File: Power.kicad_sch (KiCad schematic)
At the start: 2 parts, among them U1 LM5155DSSR, U2 LM5155DSSR

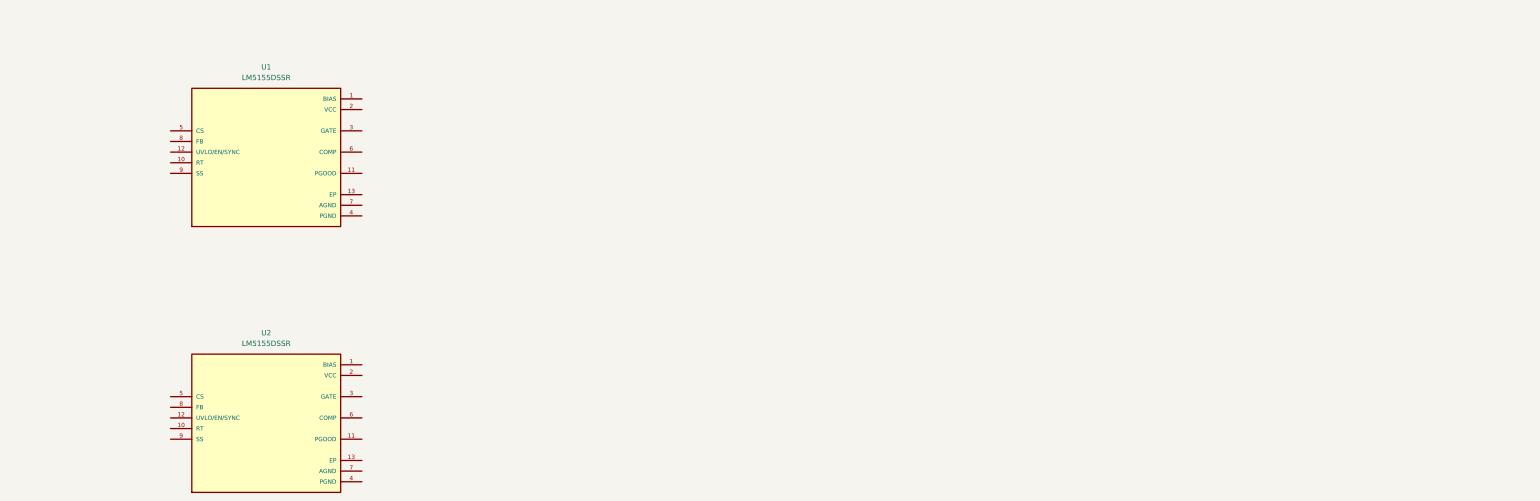
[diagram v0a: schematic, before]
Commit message: finished SOM 5V power, migrated altium stuff, finished pin study, added USB PHY (revise HS capability)
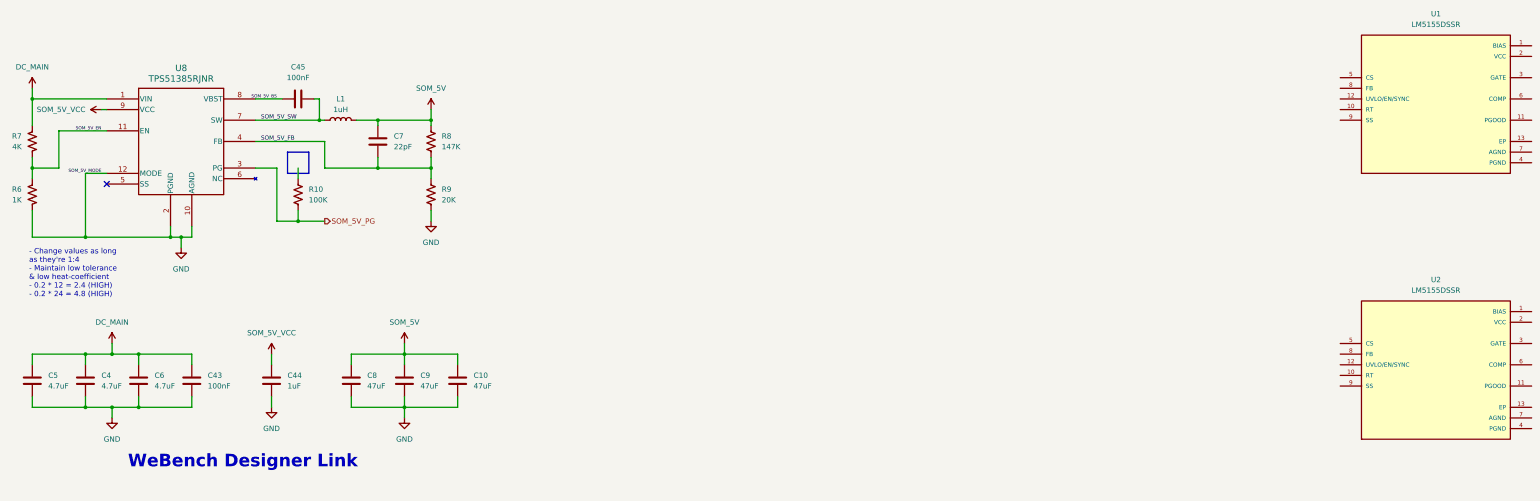
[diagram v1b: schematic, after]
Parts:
- added C10, C8, C9: 47uF, symbol Device:C
- added C4, C5, C6: 4.7uF, symbol Device:C
- added C43, C45: 100nF, symbol Device:C
- added C44: 1uF, symbol Device:C
- added C7: 22pF, symbol Device:C
- added L1: 1uH, symbol Device:L
- added R10: 100K, symbol Device:R_US
- added R6: 1K, symbol Device:R_US
- added R7: 4K, symbol Device:R_US
- added R8: 147K, symbol Device:R_US
- added R9: 20K, symbol Device:R_US
- added U8: TPS51385RJNR, VQFN-HR12_RJN_TEX, symbol TPS51385RJNR:TPS51385RJNR
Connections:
- new net DC_MAIN: C4.1, C43.1, C5.1, C6.1, R7.1, U8.1 (VIN)
- new net GND: C10.2, C4.2, C43.2, C44.2, C5.2, C6.2, C8.2, C9.2, R6.2, R9.2, U8.10 (AGND), U8.12 (MODE), U8.2 (PGND)
- new net SOM_5V: C10.1, C7.1, C8.1, C9.1, L1.2, R8.1
- new net SOM_5V_BS: C45.1, U8.8 (VBST)
- new net SOM_5V_EN: R6.1, R7.2, U8.11 (EN)
- new net SOM_5V_FB: C7.2, R8.2, R9.1, U8.4 (FB)
- new net SOM_5V_PG: R10.2, U8.3 (PG)
- new net SOM_5V_SW: C45.2, L1.1, U8.7 (SW)
- new net SOM_5V_VCC: C44.1, U8.9 (VCC)
- no-connect marks 0 -> 1
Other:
- note added: "- Change values as long as they're 1:4 - Maintain low tolerance & low heat-coefficient - 0.2 * 12 = 2.4 (HIGH) - 0.2 * 24 = 4.8 (HIGH)"
- note added: "WeBench Designer Link"
- moved on the sheet: U1, U2

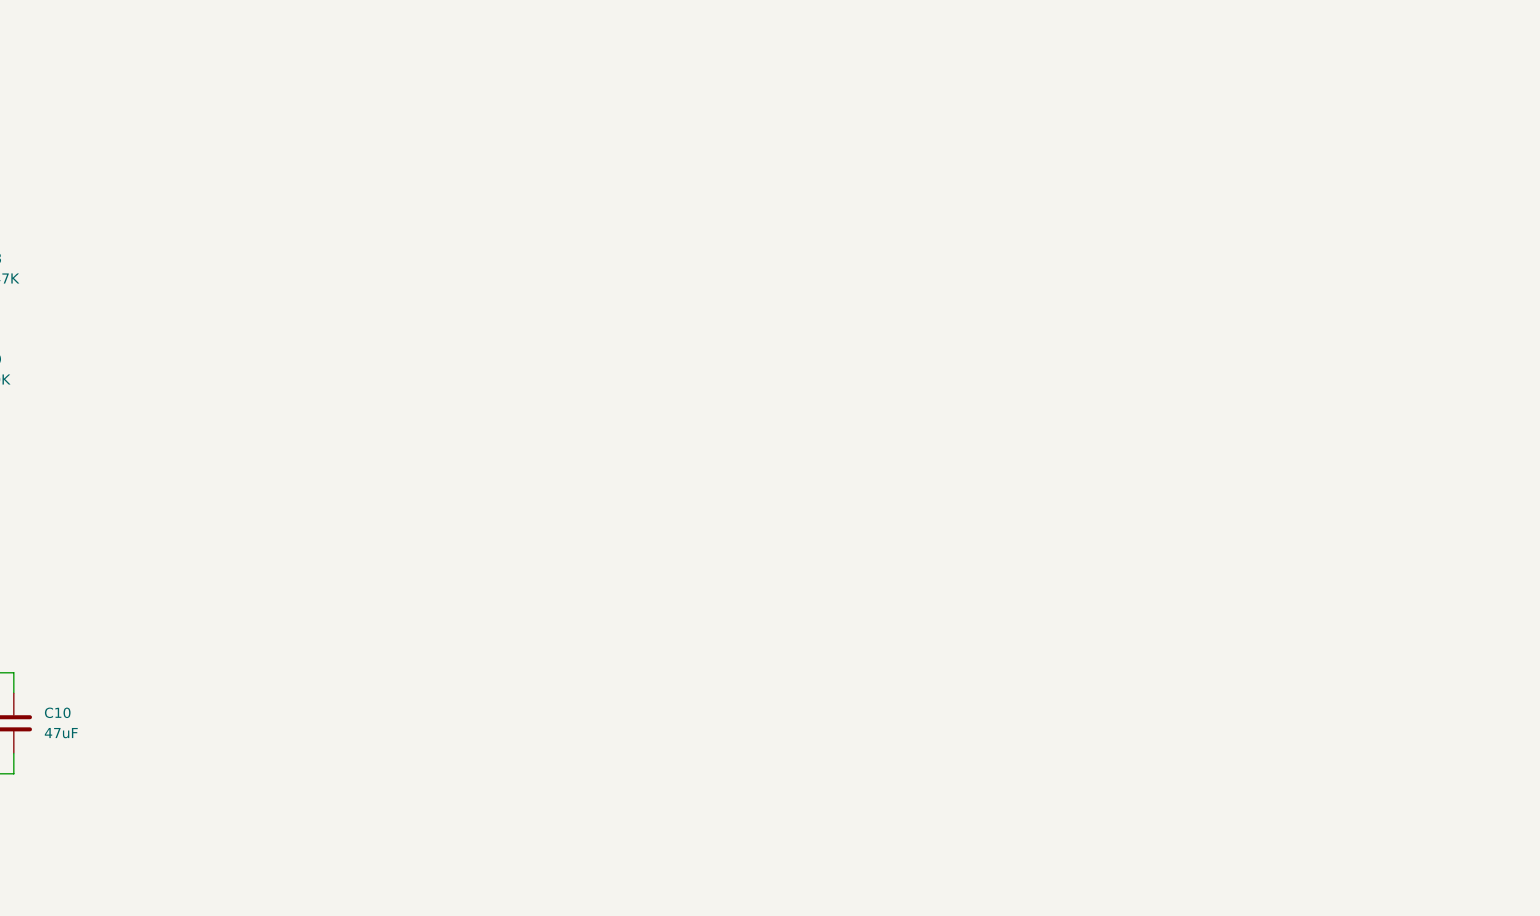
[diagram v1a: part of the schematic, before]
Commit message: added ADC clock fanout, added 3A buck
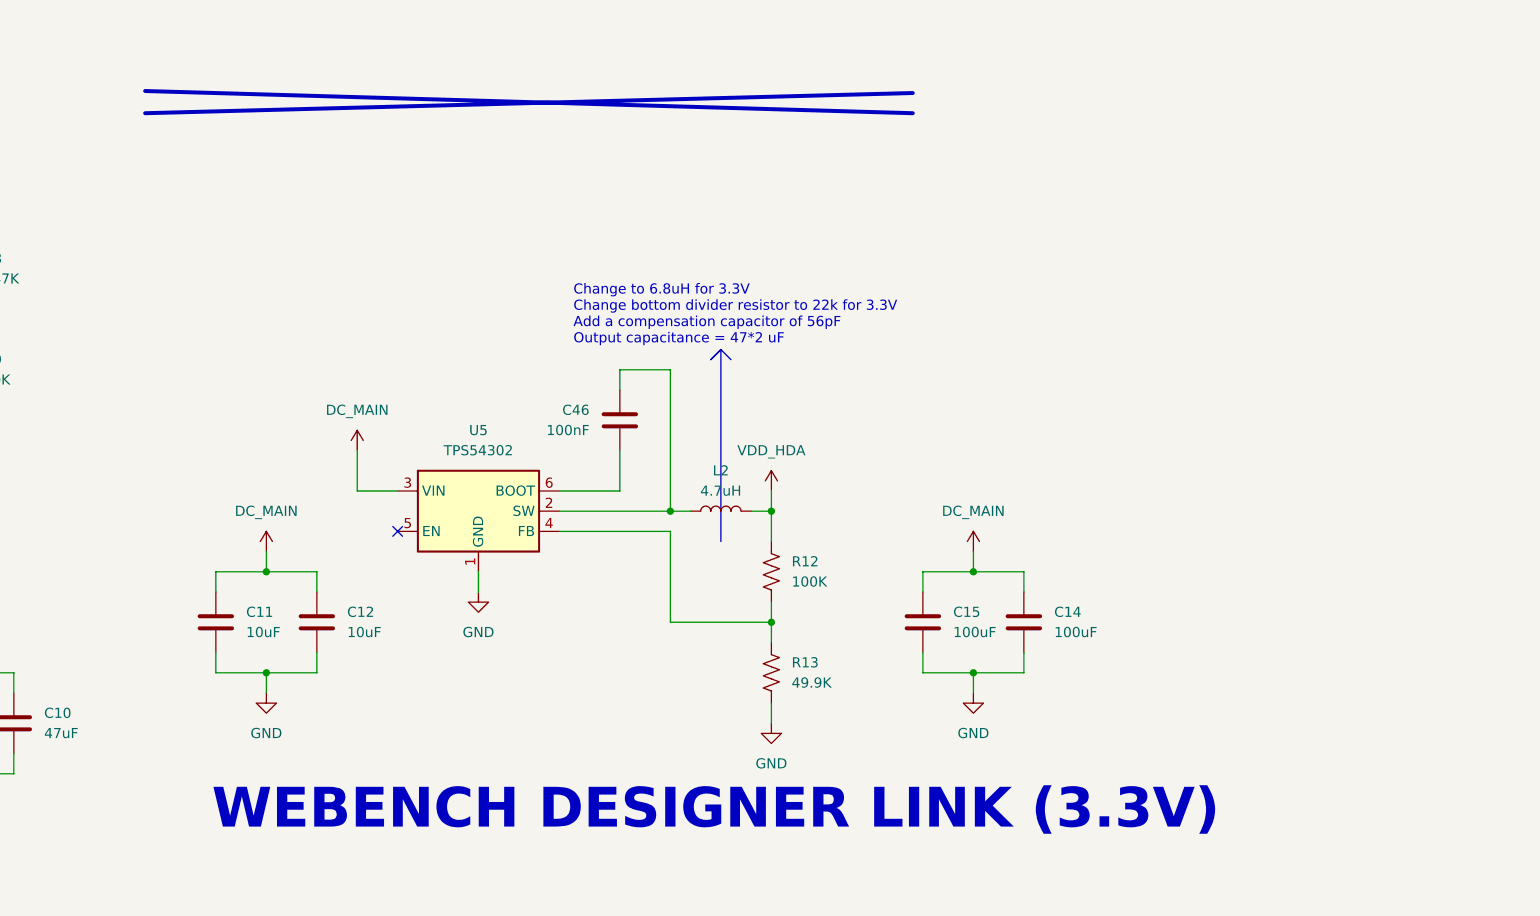
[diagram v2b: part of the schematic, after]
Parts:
- added C11, C12: 10uF, symbol Device:C
- added C14, C15: 100uF, symbol Device:C
- added C46: 100nF, symbol Device:C
- added L2: 4.7uH, symbol Device:L
- added R12: 100K, symbol Device:R_US
- added R13: 49.9K, symbol Device:R_US
- added U5: TPS54302, Package_TO_SOT_SMD:SOT-23-6, symbol Regulator_Switching:TPS54302
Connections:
- net DC_MAIN: now also C11.1, C12.1, C14.1, C15.1, U5.3 (VIN)
- net GND: now also C11.2, C12.2, C14.2, C15.2, R13.2, U5.1 (GND)
- new net: C46.2, L2.1, U5.2 (SW)
- new net: R12.2, R13.1, U5.4 (FB)
- new net: C46.1, U5.6 (BOOT)
- new net VDD_HDA: L2.2, R12.1
- no-connect marks 1 -> 2
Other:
- note added: "Change to 6.8uH for 3.3V Change bottom divider resistor to 22k for 3.3V Add a compensation capacitor of 56pF Output capacitance = 47*2 uF"
- note added: "WEBENCH DESIGNER LINK (3.3V)"

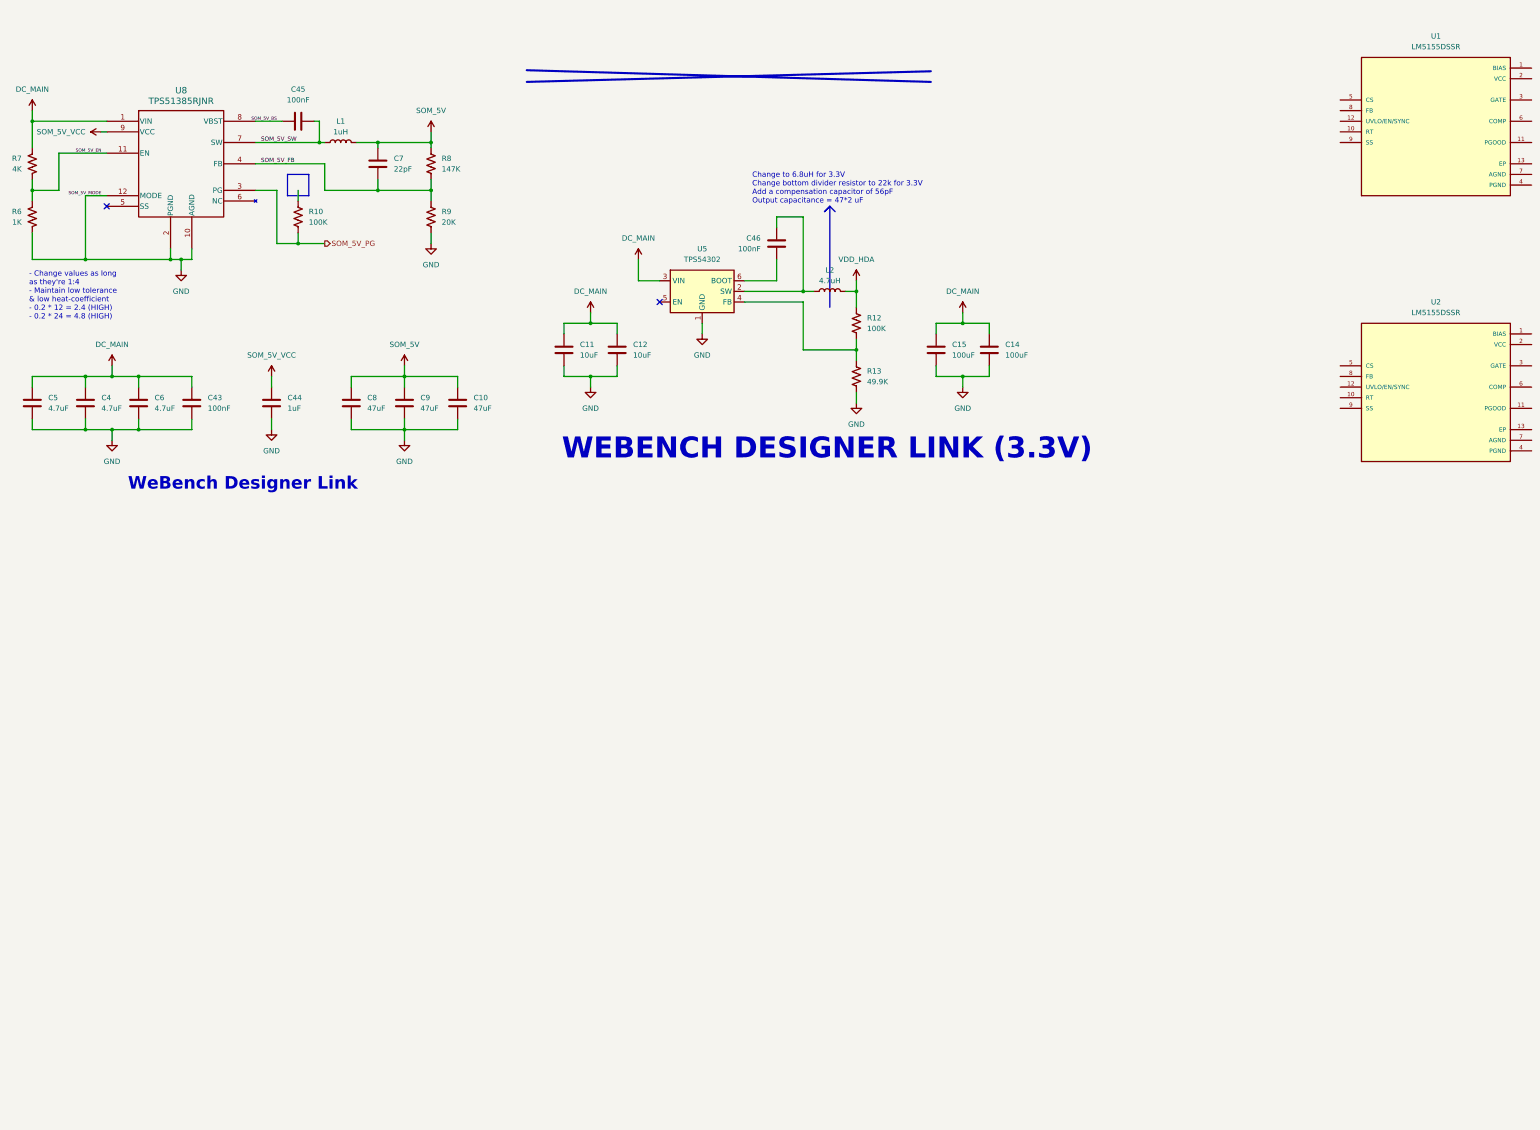
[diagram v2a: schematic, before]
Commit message: finished HV rails (revise, ai), added LDO instances, ready to bind & supply
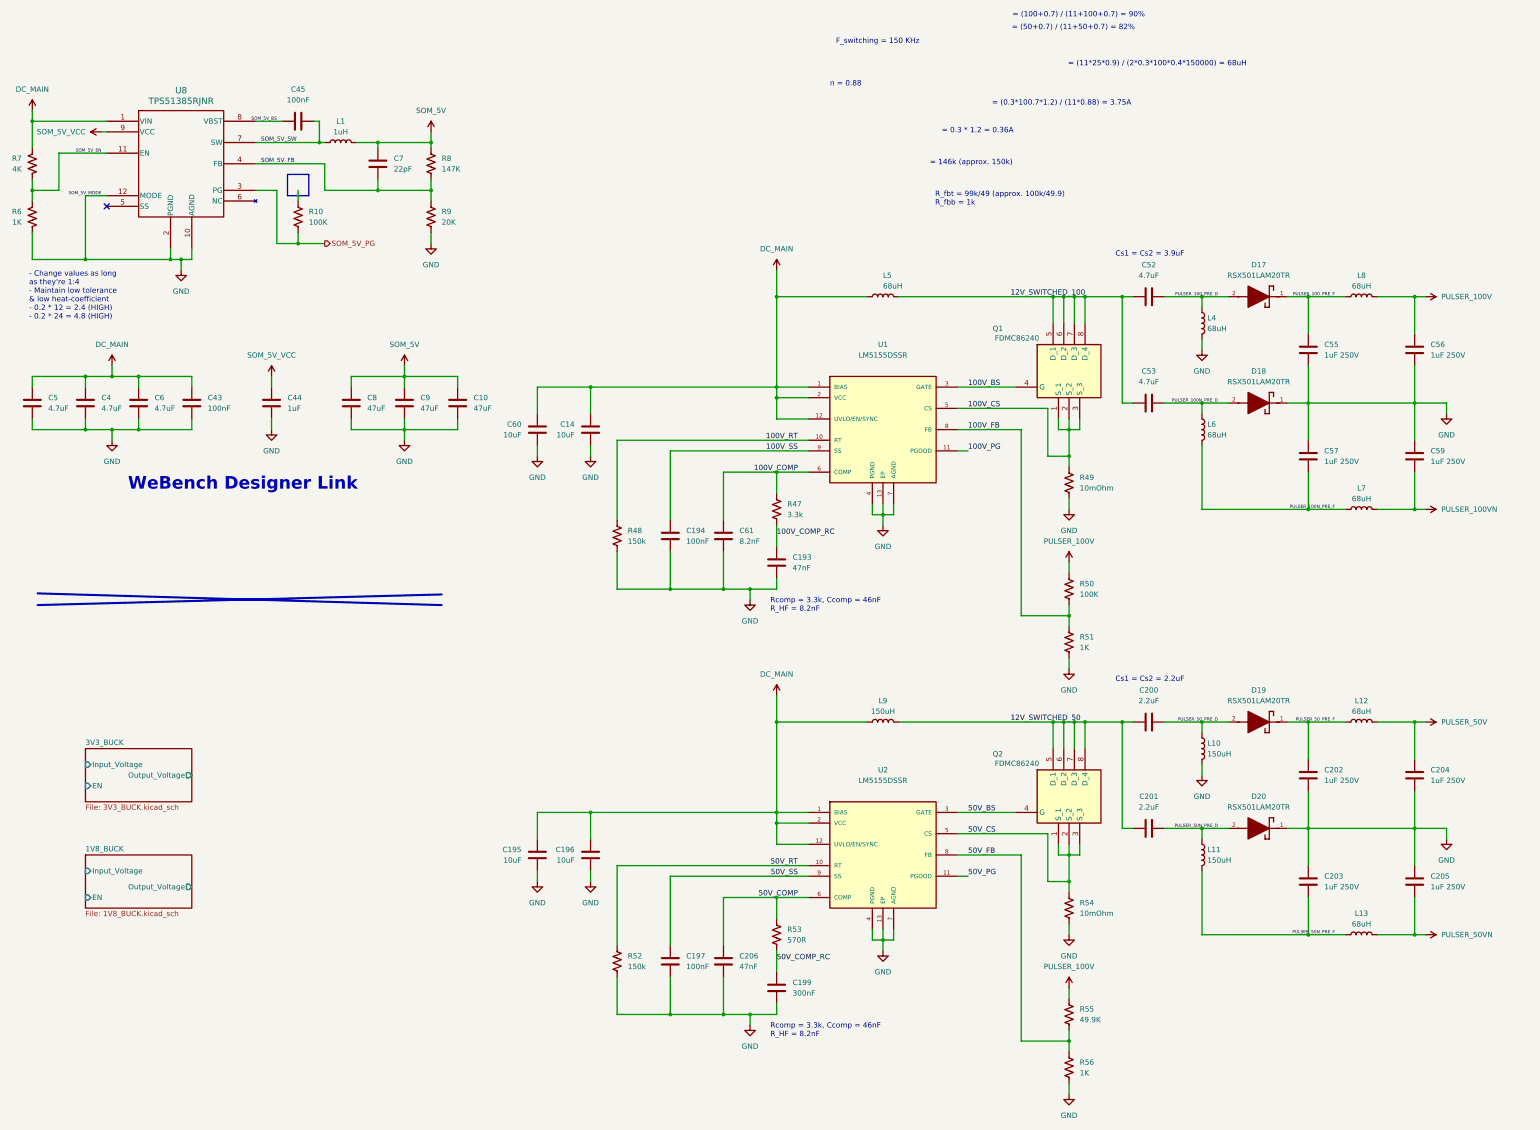
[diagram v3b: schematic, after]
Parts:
- removed C11, C12: 10uF, symbol Device:C
- removed C15: 100uF, symbol Device:C
- removed C46: 100nF, symbol Device:C
- removed L2: 4.7uH, symbol Device:L
- removed R12: 100K, symbol Device:R_US
- removed R13: 49.9K, symbol Device:R_US
- removed U5: TPS54302, Package_TO_SOT_SMD:SOT-23-6, symbol Regulator_Switching:TPS54302
- added C193, C206: 47nF, symbol Device:C
- added C194, C197: 100nF, symbol Device:C
- added C195, C196, C60: 10uF, symbol Device:C
- added C199: 300nF, symbol Device:C
- added C200, C201: 2.2uF, symbol Device:C
- added C202, C203, C204, C205, C55, C56, C57, C59: 1uF 250V, symbol Device:C
- added C52, C53: 4.7uF, symbol Device:C
- added C61: 8.2nF, symbol Device:C
- added D17, D18, D19, D20: RSX501LAM20TR, RSX501LAM20TR:DIOM4725X105N, symbol RSX501LAM20TR:RSX501LAM20TR
- added L10, L11, L9: 150uH, symbol Device:L
- added L12, L13, L4, L5, L6, L7, L8: 68uH, symbol Device:L
- added Q1, Q2: FDMC86240, FDMC86139P, symbol FDMC86240:FDMC86240
- added R47: 3.3k, symbol Device:R_US
- added R48, R52: 150k, symbol Device:R_US
- added R49, R54: 10mOhm, symbol Device:R_US
- added R50: 100K, symbol Device:R_US
- added R51, R56: 1K, symbol Device:R_US
- added R53: 570R, symbol Device:R_US
- added R55: 49.9K, symbol Device:R_US
- C14: value 100uF -> 10uF
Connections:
- net DC_MAIN: now also U1.1 (BIAS), U1.12 (UVLO/EN/SYNC), U1.2 (VCC), U2.1 (BIAS), U2.12 (UVLO/EN/SYNC), U2.2 (VCC), C195.1, C196.1, C60.1, L5.2, L9.1
- net GND: now also U1.13 (EP), U1.4 (PGND), U1.7 (AGND), U2.13 (EP), U2.4 (PGND), U2.7 (AGND), C193.2, C194.1, C195.2, C196.2, C197.1, C199.2, C202.2, C203.1, C204.2, C205.1, C206.2, C55.2, C56.2, C57.1, C59.1, C60.2, C61.2, D18.1, D20.1, L10.2, L4.2, R48.2, R49.1, R51.2, R52.2, R54.1, R56.2
- net 100V_RT: now reaches U1.10 (RT)
- net 100V_RT: now also R48.1
- net 100V_PG: now reaches U1.11 (PGOOD)
- net 100V_BS: now reaches U1.3 (GATE)
- net 100V_BS: now also Q1.4 (G)
- net 100V_CS: now reaches U1.5 (CS)
- net 100V_CS: now also Q1.1 (S_1), Q1.2 (S_2), Q1.3 (S_3), R49.2
- net 100V_COMP: now reaches U1.6 (COMP)
- net 100V_COMP: now also C61.1, R47.1
- net 100V_FB: now reaches U1.8 (FB)
- net 100V_FB: now also R50.2, R51.1
- net 100V_SS: now reaches U1.9 (SS)
- net 100V_SS: now also C194.2
- net 50V_RT: now reaches U2.10 (RT)
- net 50V_RT: now also R52.1
- net 50V_PG: now reaches U2.11 (PGOOD)
- net 50V_BS: now reaches U2.3 (GATE)
- net 50V_BS: now also Q2.4 (G)
- net 50V_CS: now reaches U2.5 (CS)
- net 50V_CS: now also Q2.1 (S_1), Q2.2 (S_2), Q2.3 (S_3), R54.2
- net 50V_COMP: now reaches U2.6 (COMP)
- net 50V_COMP: now also C206.1, R53.1
- net 50V_FB: now reaches U2.8 (FB)
- net 50V_FB: now also R55.2, R56.1
- net 50V_SS: now reaches U2.9 (SS)
- net 50V_SS: now also C197.2
- new net 100V_COMP_RC: C193.1, R47.2
- new net 12V_SWITCHED_100: C52.1, C53.1, L5.1, Q1.5 (D_1), Q1.6 (D_2), Q1.7 (D_3), Q1.8 (D_4)
- new net 12V_SWITCHED_50: C200.1, C201.1, L9.2, Q2.5 (D_1), Q2.6 (D_2), Q2.7 (D_3), Q2.8 (D_4)
- new net 50V_COMP_RC: C199.1, R53.2
- new net PULSER_100N_PRE_D: C53.2, D18.2, L6.1
- new net PULSER_100N_PRE_F: C57.2, L6.2, L7.1
- new net PULSER_100V: C56.1, L8.2, R50.1, R55.1
- new net PULSER_100VN: C59.2, L7.2
- new net PULSER_100_PRE_D: C52.2, D17.2, L4.1
- new net PULSER_100_PRE_F: C55.1, D17.1, L8.1
- new net PULSER_50N_PRE_D: C201.2, D20.2, L11.1
- new net PULSER_50N_PRE_F: C203.2, L11.2, L13.1
- new net PULSER_50V: C204.1, L12.2
- new net PULSER_50VN: C205.2, L13.2
- new net PULSER_50_PRE_D: C200.2, D19.2, L10.1
- new net PULSER_50_PRE_F: C202.1, D19.1, L12.1
- no-connect marks 2 -> 1
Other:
- added sheet 1V8_BUCK (1V8_BUCK.kicad_sch)
- added sheet 3V3_BUCK (3V3_BUCK.kicad_sch)
- note added: "= (0.3*100.7*1.2) / (11*0.88) = 3.75A"
- note added: "= (100+0.7) / (11+100+0.7) = 90%"
- note added: "= (11*25*0.9) / (2*0.3*100*0.4*150000) = 68uH"
- note added: "= (50+0.7) / (11+50+0.7) = 82%"
- note added: "= 0.3 * 1.2 = 0.36A"
- note added: "= 146k (approx. 150k)"
- note added: "Cs1 = Cs2 = 2.2uF"
- note added: "Cs1 = Cs2 = 3.9uF"
- note added: "F_switching = 150 KHz"
- note added: "R_fbt = 99k/49 (approx. 100k/49.9) R_fbb = 1k"
- note added: "Rcomp = 3.3k, Ccomp = 46nF R_HF = 8.2nF"
- note added: "n = 0.88"
- note removed: "Change to 6.8uH for 3.3V Change bottom divider resistor to 22k for 3.3V Add a compensation capacitor of 56pF Output capacitance = 47*2 uF"
- note removed: "WEBENCH DESIGNER LINK (3.3V)"
- moved on the sheet: U1

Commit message: added USB (needs revision), fixed medium voltage rail
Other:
- sheet 1V8_BUCK renamed TX1V8
- added sheet USB_1V8 (1V8_BUCK.kicad_sch)
